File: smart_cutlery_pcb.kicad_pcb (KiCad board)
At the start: 2 copper layers, 95 x 19.5 mm, 80 parts, among them J1 CONN_01X05, J2 CONN_01X04, Q1 BSS84, Q2 BSS138, SW1 TL3342, U1 STM32L053C6Tx, U2 MODULE-BLUETOOTH-HC-05(34P-27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, U3 NCP1402SN33T1G, U4 MPU-9250, U5 ASMT-YTC2-0AA02

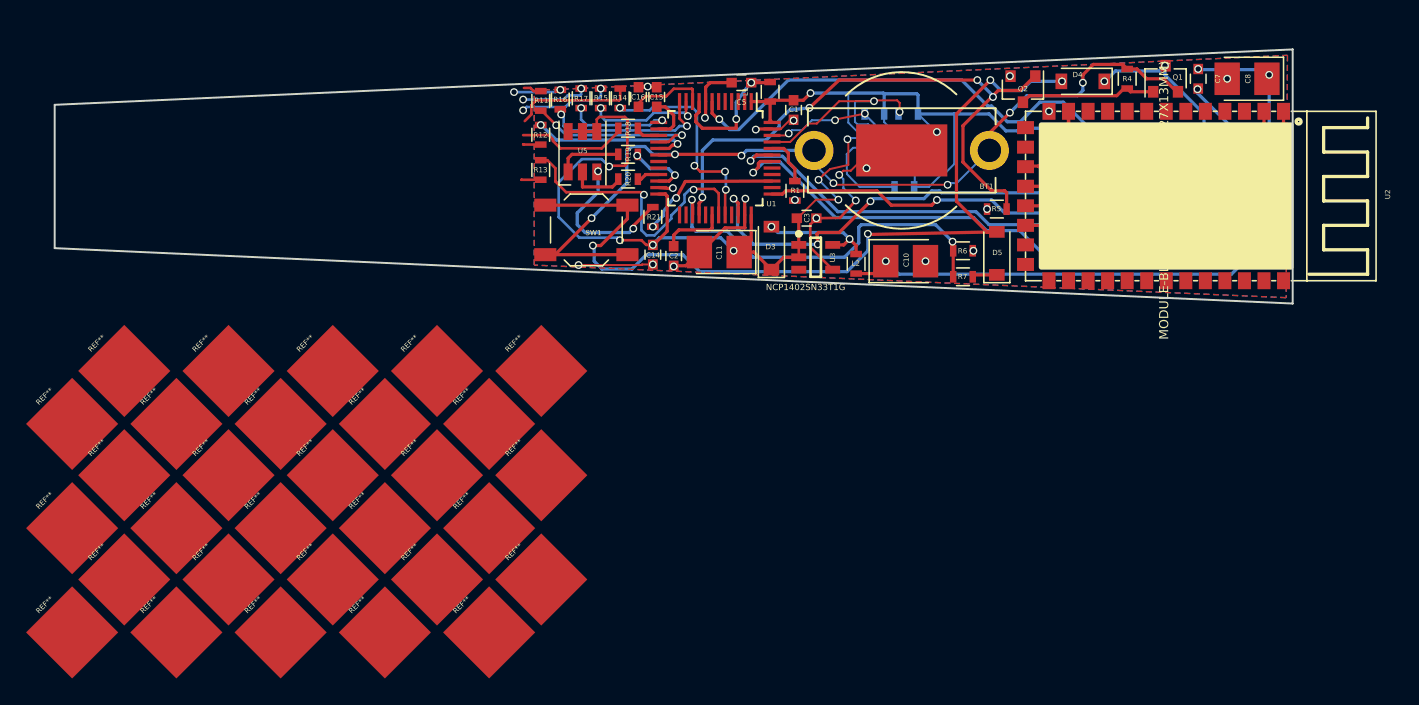
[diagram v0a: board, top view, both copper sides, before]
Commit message: Finish touch pattern (rev1), ground hatching, gerbers r1
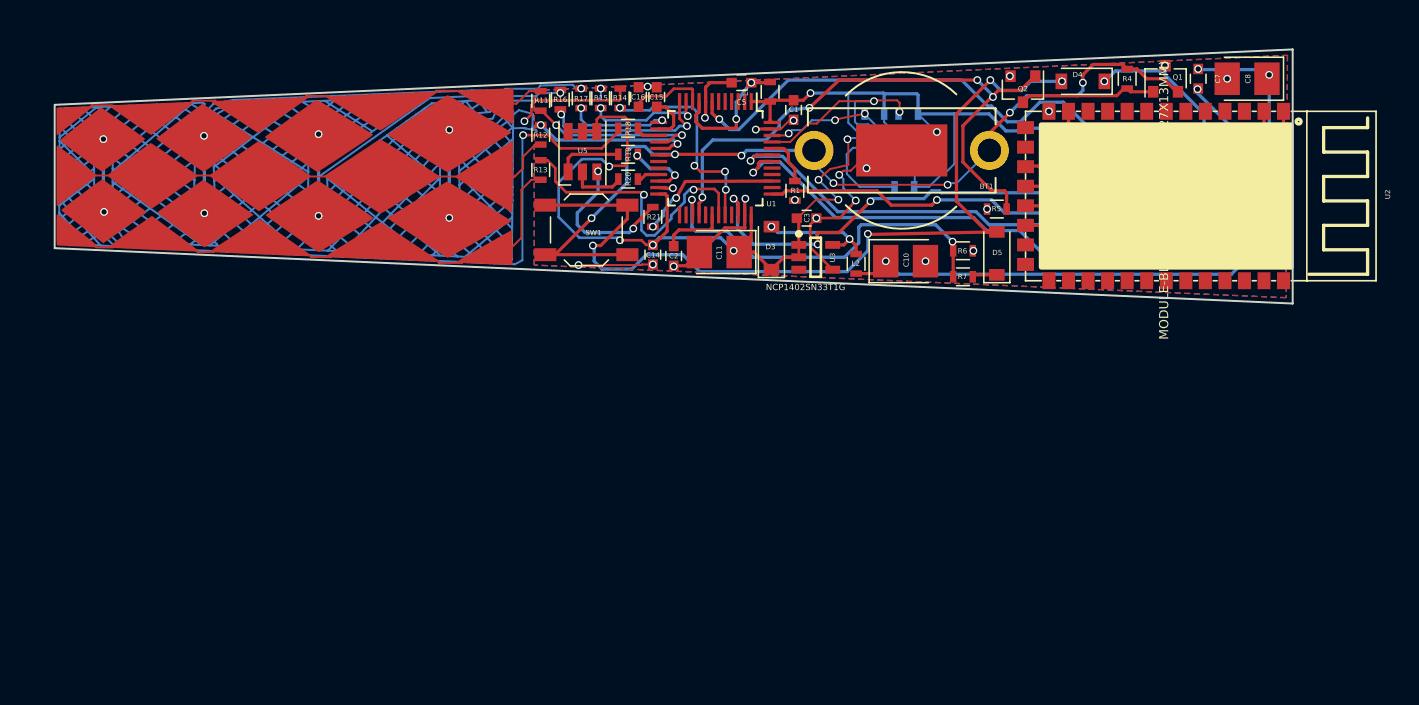
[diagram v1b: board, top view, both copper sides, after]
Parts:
- removed REF** (x30): Measurement_Point_Square-SMD-Pad_Big, Measurement_Points:Measurement_Point_Square-SMD-Pad_Big
- added G***: LOGO, smart_cutlery_pcb:touch_pattern_1, F.Cu at (121.2, 71.5)
- added REF***: OSHW-Logo2_7.3x6mm_SilkScreen, Symbols:OSHW-Logo2_7.3x6mm_SilkScreen, B.Cu at (107.2, 69.0)
- added REF***: ESD-Logo_6.6x6mm_SilkScreen, Symbols:ESD-Logo_6.6x6mm_SilkScreen, B.Cu at (135.1, 74.7)
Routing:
- net (no net): track 0.00 -> 991.3 mm
- net /touch_interface/sense_x4: track 8.60 -> 57.9 mm, vias 0 -> 3
- net /touch_interface/sense_x3: track 5.07 -> 37.3 mm, vias 2 -> 3
- net /touch_interface/sense_x2: track 3.63 -> 30.5 mm, vias 2 -> 3
- net /touch_interface/sense_x1: track 7.19 -> 20.5 mm, vias 2 -> 3
- net /touch_interface/sense_y3: track 1.48 -> 6.92 mm
- net /touch_interface/sense_y2: track 1.36 -> 4.41 mm
- net /touch_interface/sense_y1: track 1.39 -> 3.02 mm
- net GND: track 59.0 -> 60.2 mm
- net /touch_interface/sense_y4: track 9.25 -> 9.28 mm, vias 0 -> 1
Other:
- board text added: "CutleryController"
- board text added: "Rev. 1A"
- board text added: "S. HOLZAPFEL, J. WINDEYER 2017"

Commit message: Increase outline by 0.2mm on all sides to pass audit
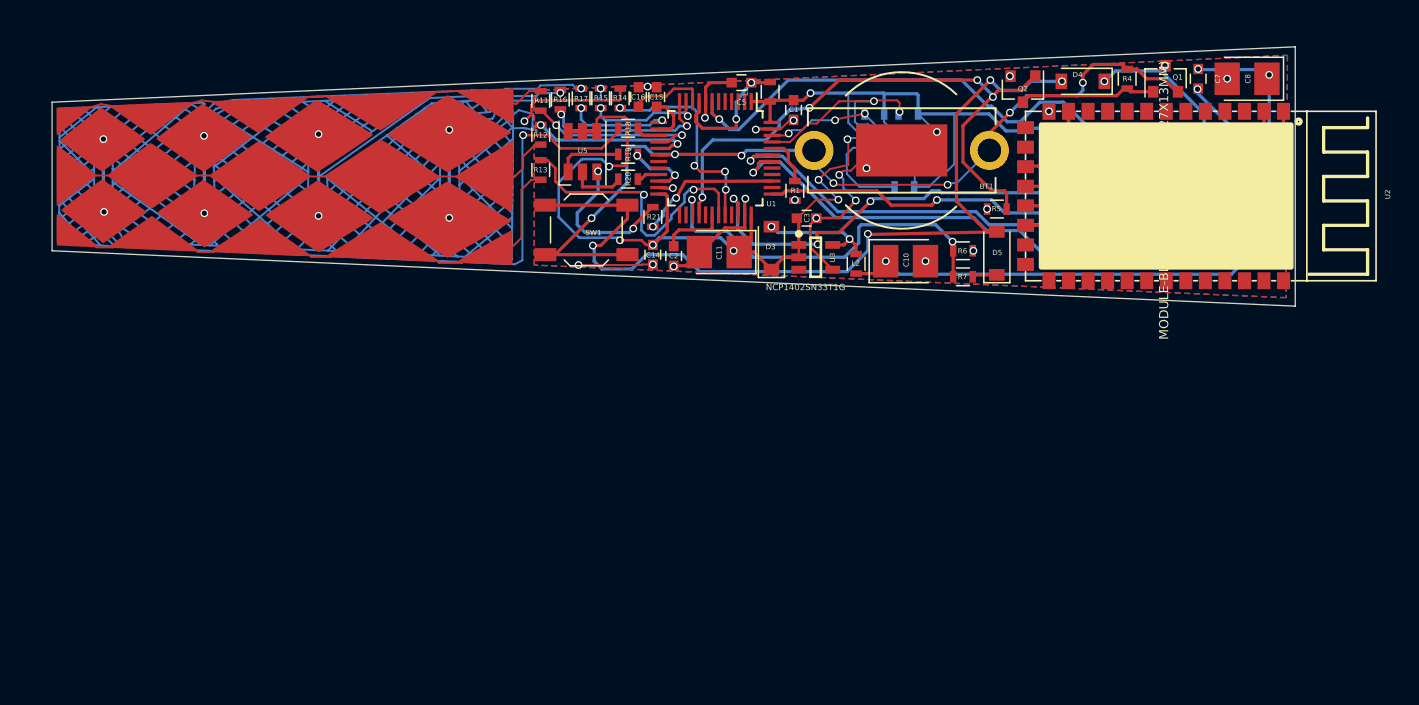
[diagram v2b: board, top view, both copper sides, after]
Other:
- board size 95 x 19.5 mm -> 95.4 x 19.9 mm
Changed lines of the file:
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@@
     (links 110)
     (no_connects 0)
-    (area 103.424999 61.674999 198.575001 81.325001)
+    (area 93.30283 59.923 206.3063 85.594121)
     (thickness 1.6)
     (drawings 7)
@@
   )
   (setup
-    (last_trace_width 0.1524)
+    (last_trace_width 0.25)
     (user_trace_width 0.1524)
     (user_trace_width 0.2032)
@@
     (effects (font (size 0.8 0.8) (thickness 0.2)) (justify mirror))
   )
-  (gr_line (start 198.5 81.25) (end 198.5 61.75) (angle 90) (layer Edge.Cuts) (width 0.15))
-  (gr_line (start 103.5 77) (end 103.5 66) (angle 90) (layer Edge.Cuts) (width 0.15))
-  (gr_line (start 103.5 77) (end 198.5 81.25) (angle 90) (layer Edge.Cuts) (width 0.15))
-  (gr_line (start 103.5 66) (end 198.5 61.75) (angle 90) (layer Edge.Cuts) (width 0.15))
+  (gr_line (start 198.7 81.45) (end 198.7 61.55) (angle 90) (layer Edge.Cuts) (width 0.01))
+  (gr_line (start 103.3 77.2) (end 103.3 65.8) (angle 90) (layer Edge.Cuts) (width 0.01))
+  (gr_line (start 103.3 77.2) (end 198.7 81.45) (angle 90) (layer Edge.Cuts) (width 0.01))
+  (gr_line (start 103.3 65.8) (end 198.7 61.55) (angle 90) (layer Edge.Cuts) (width 0.01))
   (segment (start 134.483741 68.549725) (end 135.620881 67.678811) (width 0.1524) (layer B.Cu) (net 0))
   (segment (start 134.497868 69.190149) (end 137.149652 67.494304) (width 0.1524) (layer B.Cu) (net 0))
@@
   (segment (start 104.801998 76.539886) (end 104.909778 76.670363) (width 0.1524) (layer B.Cu) (net 0))
   (segment (start 132.5372 65.1256) (end 132.588 65.1256) (width 0.1524) (layer F.Cu) (net 0))
-  (segment (start 132.7912 64.9224) (end 134.62 64.9224) (width 0.1524) (layer F.Cu) (net 0))
-  (segment (start 132.588 65.1256) (end 132.7912 64.9224) (width 0.1524) (layer F.Cu) (net 0))
+  (segment (start 132.78104 65.00876) (end 134.62 64.9224) (width 0.1524) (layer F.Cu) (net 0))
+  (segment (start 132.588 65.1256) (end 132.78104 65.00876) (width 0.1524) (layer F.Cu) (net 0))
   (segment (start 122.428 65.532) (end 122.6058 65.532) (width 0.1524) (layer F.Cu) (net 0))
-  (segment (start 122.809 65.3288) (end 124.587 65.3288) (width 0.1524) (layer F.Cu) (net 0))
-  (segment (start 122.6058 65.532) (end 122.809 65.3288) (width 0.1524) (layer F.Cu) (net 0))
+  (segment (start 122.8344 65.405) (end 124.587 65.3288) (width 0.1524) (layer F.Cu) (net 0))
+  (segment (start 122.6058 65.532) (end 122.8344 65.405) (width 0.1524) (layer F.Cu) (net 0))
   (segment (start 113.8174 65.913) (end 113.8682 65.913) (width 0.1524) (layer F.Cu) (net 0))
-  (segment (start 115.824 65.6844) (end 115.951 65.8114) (width 0.1524) (layer F.Cu) (net 0))
-  (segment (start 114.0968 65.6844) (end 115.824 65.6844) (width 0.1524) (layer F.Cu) (net 0))
-  (segment (start 113.8682 65.913) (end 114.0968 65.6844) (width 0.1524) (layer F.Cu) (net 0))
+  (segment (start 115.824 65.77584) (end 115.951 65.8114) (width 0.1524) (layer F.Cu) (net 0))
+  (segment (start 114.79276 65.66916) (end 115.824 65.77584) (width 0.1524) (layer F.Cu) (net 0))
+  (segment (start 113.8682 65.913) (end 114.79276 65.66916) (width 0.1524) (layer F.Cu) (net 0))
   (segment (start 106.1466 66.2178) (end 106.172 66.2178) (width 0.1524) (layer F.Cu) (net 0))
-  (segment (start 106.3498 66.04) (end 107.9246 66.04) (width 0.1524) (layer F.Cu) (net 0))
-  (segment (start 106.172 66.2178) (end 106.3498 66.04) (width 0.1524) (layer F.Cu) (net 0))
+  (segment (start 107.04068 65.95364) (end 107.96524 66.10604) (width 0.1524) (layer F.Cu) (net 0))
+  (segment (start 106.172 66.2178) (end 107.04068 65.95364) (width 0.1524) (layer F.Cu) (net 0))
   (segment (start 132.7658 77.9272) (end 132.7912 77.9272) (width 0.1524) (layer F.Cu) (net 0))
   (segment (start 134.747 78.1304) (end 134.9248 77.9526) (width 0.1524) (layer F.Cu) (net 0))

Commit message: Finish pattern b, get fabbed
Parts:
- removed G***: LOGO, smart_cutlery_pcb:touch_pattern_1
- removed the REF*** at (107.2, 69.0)
- removed the REF*** at (135.1, 74.7)
- added REF***: OSHW-Logo_5.7x6mm_SilkScreen, Symbols:OSHW-Logo_5.7x6mm_SilkScreen, B.Cu at (107.7, 71.0)
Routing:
- net (no net): track 991.1 -> 794.5 mm
- net /touch_interface/sense_y1: track 3.02 -> 36.4 mm
- net /touch_interface/sense_y2: track 4.41 -> 19.9 mm, vias 0 -> 2
- net /touch_interface/sense_x4: track 57.9 -> 44.2 mm, vias 3 -> 2
- net /touch_interface/sense_x3: track 37.3 -> 47.1 mm, vias 3 -> 2
- net /touch_interface/sense_y4: track 9.28 -> 14.6 mm, vias 1 -> 0
- net /touch_interface/sense_x2: track 30.5 -> 34.3 mm, vias 3 -> 2
- net /touch_interface/sense_x1: track 20.5 -> 19.3 mm, vias 3 -> 2
- net /touch_interface/sense_y3: track 6.92 -> 7.60 mm, vias 0 -> 2
- added copper zone on F.Cu, net /touch_interface/sense_x1
- added copper zone on F.Cu, net /touch_interface/sense_x2
- added copper zone on F.Cu, net /touch_interface/sense_x3
- added copper zone on F.Cu, net /touch_interface/sense_x4
- added copper zone on F.Cu, net /touch_interface/sense_y1
- added copper zone on F.Cu, net /touch_interface/sense_y2
- added copper zone on F.Cu, net /touch_interface/sense_y3
- added copper zone on F.Cu, net /touch_interface/sense_y4
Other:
- board text added: "Rev. 1A (Directional)"
- board text removed: "Rev. 1A"
